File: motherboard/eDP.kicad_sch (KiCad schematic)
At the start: 1 part, among them J9 20455-040E-12 IPEX OLED

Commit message: implemented most features
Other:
- moved on the sheet: J9

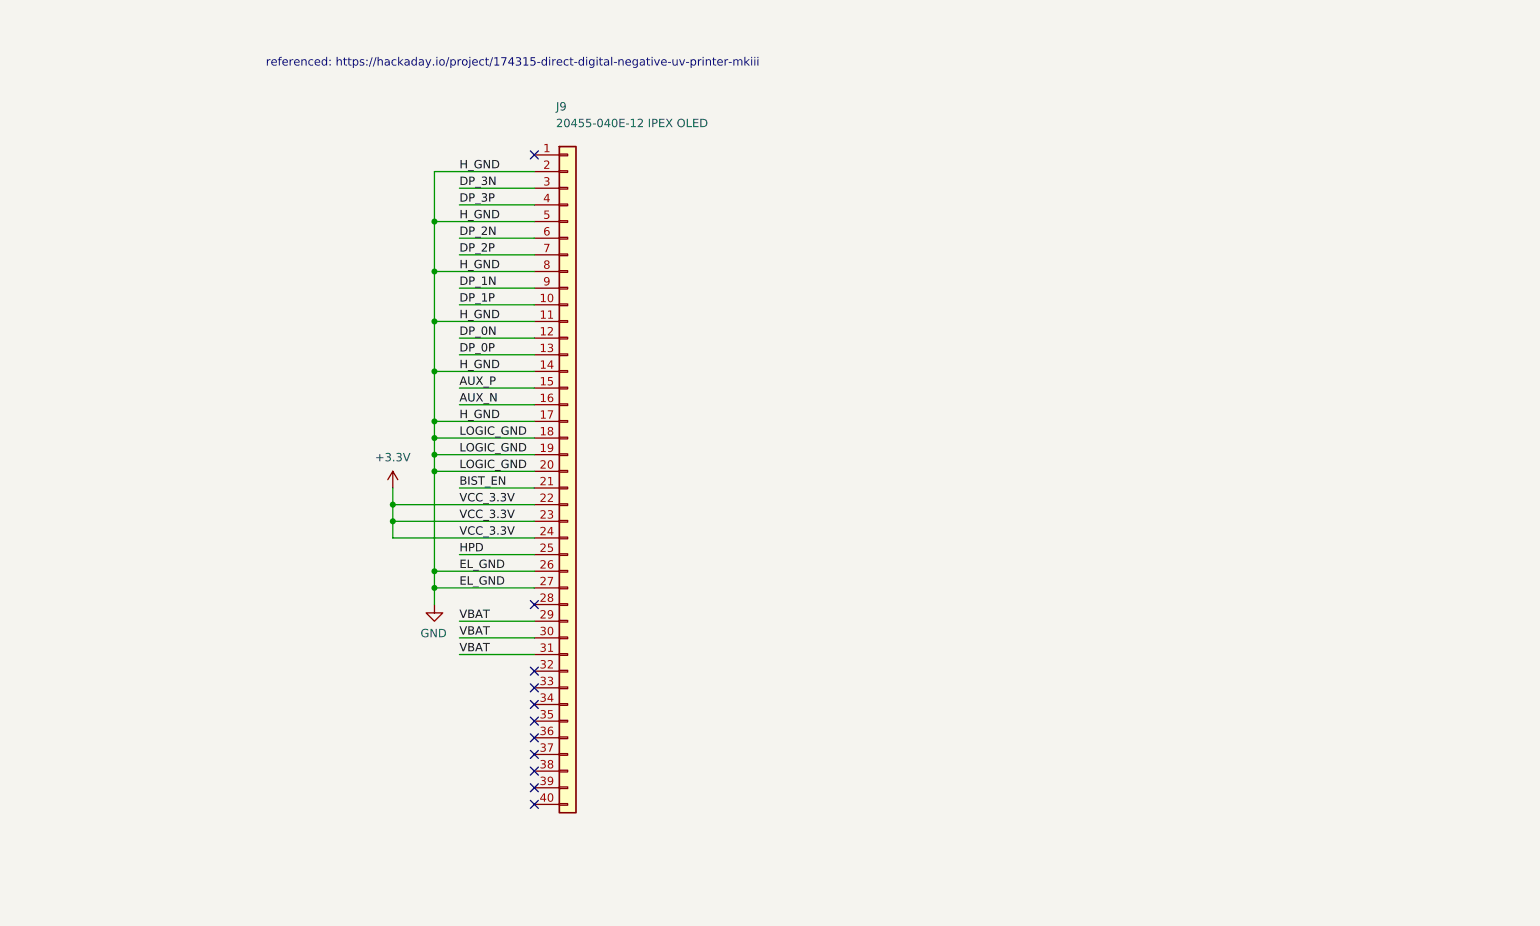
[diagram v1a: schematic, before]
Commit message: linked all footprints
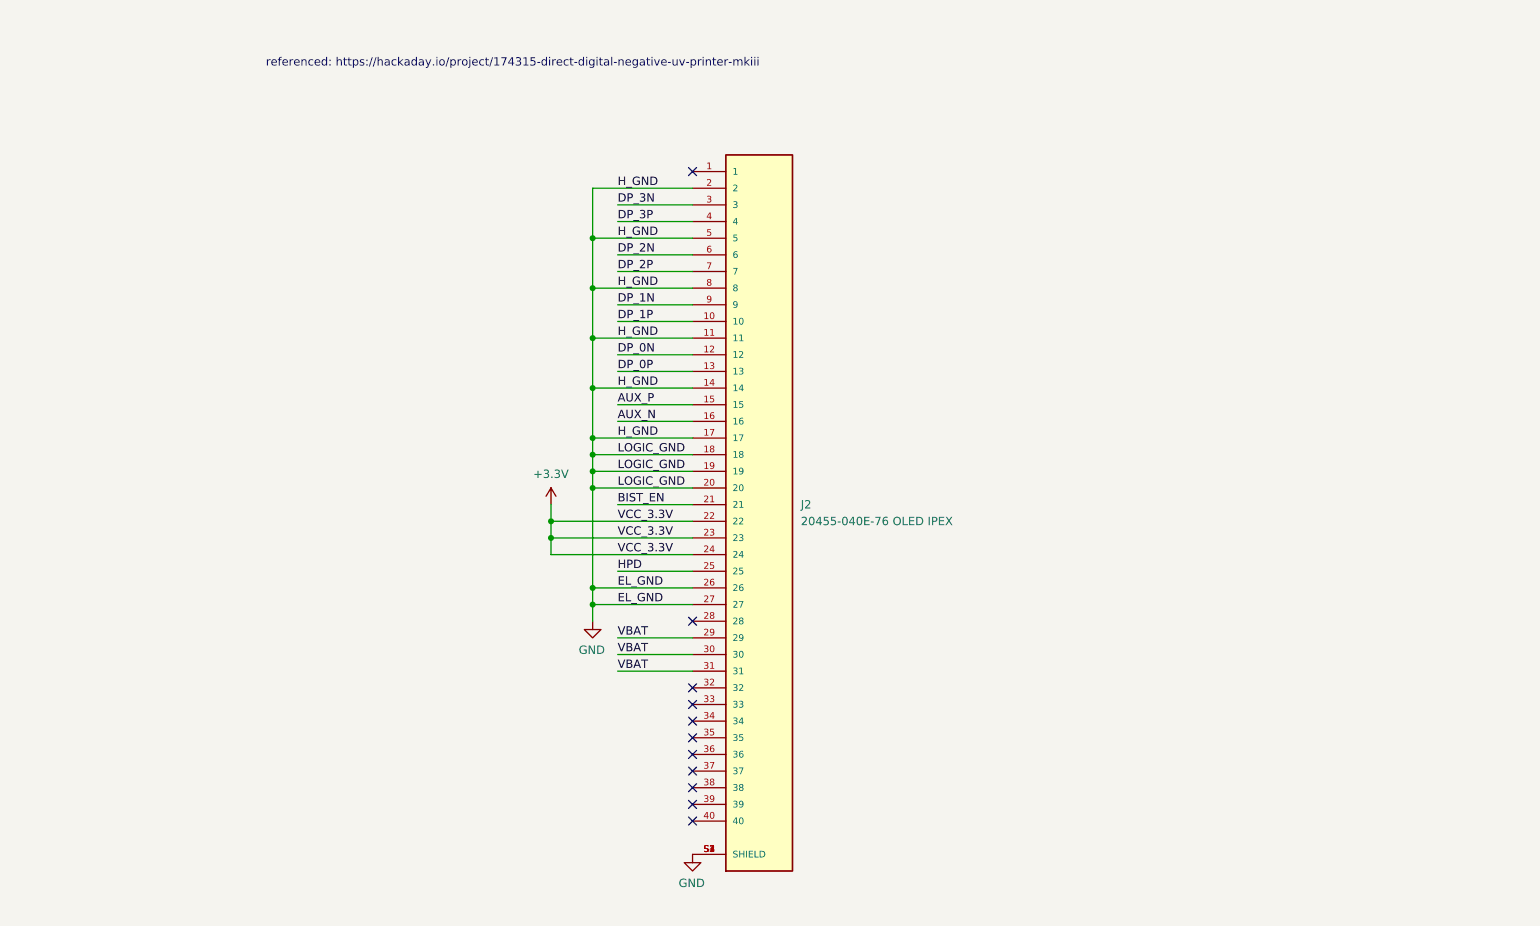
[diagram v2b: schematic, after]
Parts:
- removed J9: 20455-040E-12 IPEX OLED, symbol Connector_Generic:Conn_01x40
- added J2: 20455-040E-76 OLED IPEX, eDP_Connector:IPEX_20455-040E-76, symbol eDP_Connector:20455-040E-76
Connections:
- net +3.3V: now also J2.22, J2.23, J2.24
- net AUX_N: now also J2.16
- net AUX_P: now also J2.15
- net BIST_EN: now also J2.21
- net DP_0N: now also J2.12
- net DP_0P: now also J2.13
- net DP_1N: now also J2.9
- net DP_1P: now also J2.10
- net DP_2N: now also J2.6
- net DP_2P: now also J2.7
- net DP_3N: now also J2.3
- net DP_3P: now also J2.4
- net GND: now also J2.11, J2.14, J2.17, J2.18, J2.19, J2.2, J2.20, J2.26, J2.27, J2.5, J2.8, J2.S1 (SHIELD), J2.S2 (SHIELD), J2.S3 (SHIELD), J2.S4 (SHIELD)
- net HPD: now also J2.25
- net VBAT: now also J2.29, J2.30, J2.31

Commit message: motherboard schematic done
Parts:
- added J6: OLED EL POWER, 6P_05mm_FPC:FPC-SMD_6P-P0.50_XUNPU_FPC-05F-6PH20, symbol Connector_Generic:Conn_01x06
- added R120, R121: 0R, Resistor_SMD:R_0402_1005Metric, symbol Device:R_Small
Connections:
- net +3.3V: now also R121.1
- net BIST_EN: now also R120.1; no longer J2.21
- net GND: now also J6.1 (Pin_1), J6.2 (Pin_2), J6.3 (Pin_3)
- net HPD: no longer names the net of J2.25
- net HPD: now also R121.2
- net VBAT: no longer names the net of J2.29, J2.30, J2.31
- net VBAT: now also J6.4 (Pin_4), J6.5 (Pin_5), J6.6 (Pin_6)
- new net: J2.21, R120.2
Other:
- note added: "built in self test?"
- moved on the sheet: J2

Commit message: work preparing for routing
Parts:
- J6: symbol Connector_Generic:Conn_01x06 -> Connector_Generic_MountingPin:Conn_01x06_MountingPin
- R120: now not fitted
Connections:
- net GND: now also J6.MP (MountPin)
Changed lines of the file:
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@@
 		(in_bom yes)
 		(on_board yes)
-		(dnp no)
+		(dnp yes)
 		(fields_autoplaced yes)
 		(property "Reference" "R120"
@@
 	)
 	(symbol
-		(lib_id "Connector_Generic:Conn_01x06")
+		(lib_id "Connector_Generic_MountingPin:Conn_01x06_MountingPin")
 		(at 124.46 128.27 180)
 		(unit 1)
@@
 		(fields_autoplaced yes)
 		(property "Reference" "J6"
-			(at 124.46 114.3 0)
+			(at 121.92 125.3743 0)
 			(effects
 				(font
 					(size 1.27 1.27)
 				)
+				(justify left)
 			)
 		)
 		(property "Value" "OLED EL POWER"
-			(at 124.46 116.84 0)
+			(at 121.92 127.9143 0)
 			(effects
 				(font
 					(size 1.27 1.27)
 				)
+				(justify left)
 			)
 		)
@@
 		(pin "4"
 		)
+		(pin "MP"
+		)
 		(instances
 			(project ""
@@
 					(unit 1)
 				)
+			)
+		)
+	)
+	(symbol
+		(lib_id "eDP_adaptor_board-rescue:GND-power")
+		(at 124.46 115.57 0)
+		(mirror x)
+		(unit 1)
+		(exclude_from_sim no)
+		(in_bom yes)
+		(on_board yes)
+		(dnp no)
+		(property "Reference" "#PWR0161"
+			(at 124.46 109.22 0)
+			(effects
+				(font
+					(size 1.27 1.27)
+				)
+				(hide yes)
+			)
+		)
+		(property "Value" "GND"
+			(at 128.016 113.03 0)
+			(effects
+				(font
+					(size 1.27 1.27)
+				)
+			)
+		)
+		(property "Footprint" ""
+			(at 124.46 115.57 0)
+			(effects
+				(font
+					(size 1.27 1.27)
+				)
+				(hide yes)
+			)
+		)
+		(property "Datasheet" ""
+			(at 124.46 115.57 0)
+			(effects
+				(font
+					(size 1.27 1.27)
+				)
+				(hide yes)
+			)
+		)
+		(property "Description" ""
+			(at 124.46 115.57 0)
+			(effects
+				(font
+					(size 1.27 1.27)
+				)
+			)
+		)
+		(pin "1"
+		)
+		(instances
+			(project "motherboard"
+				(path "/025fe4d1-0305-4b34-be04-f8d9818125a4/41516588-89d4-4c4a-8d7d-a4354a401e31"
+					(reference "#PWR0161")
+					(unit 1)
+				)

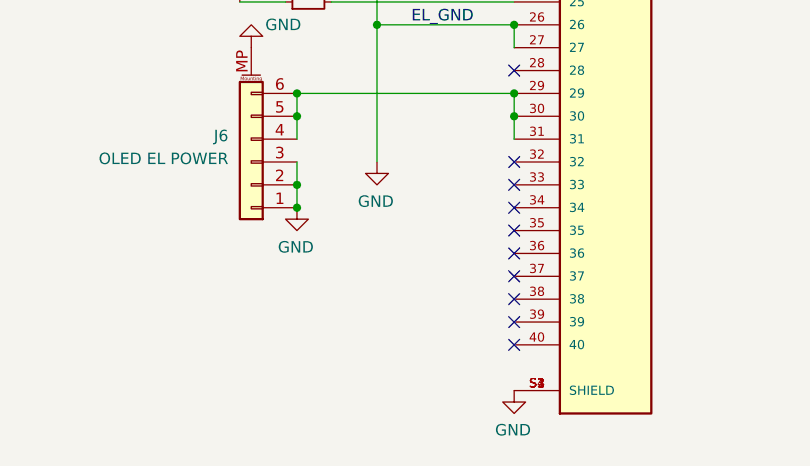
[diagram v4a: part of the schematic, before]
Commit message: component placement of I/O
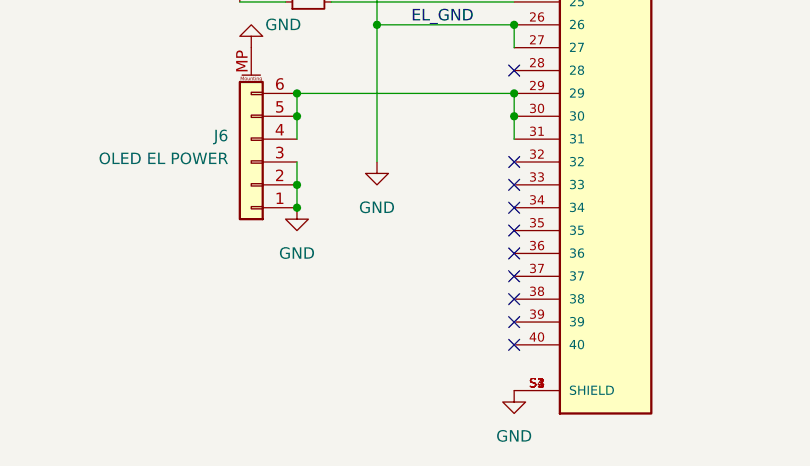
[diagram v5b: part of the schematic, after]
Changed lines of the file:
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@@
+	)
+	(junction
+		(at 129.54 133.35)
+		(diameter 0)
+		(color 0 0 0 0)
 	)
 	(junction
@@
 	)
 	(junction
-		(at 129.54 133.35)
-		(diameter 0)
-		(color 0 0 0 0)
-	)
-	(junction
 		(at 153.67 107.95)
 		(diameter 0)
@@
 	)
 	(symbol
-		(lib_id "eDP_adaptor_board-rescue:GND-power")
-		(at 129.54 133.35 0)
-		(mirror y)
+		(lib_id "power:GND")
+		(at 138.43 128.27 0)
 		(unit 1)
 		(exclude_from_sim no)
@@
 		(on_board yes)
 		(dnp no)
-		(property "Reference" "#PWR0145"
-			(at 129.54 139.7 0)
+		(fields_autoplaced yes)
+		(property "Reference" "#PWR057"
+			(at 138.43 134.62 0)
 			(effects
 				(font
@@
 		)
 		(property "Value" "GND"
-			(at 129.413 137.7442 0)
+			(at 138.43 133.35 0)
 			(effects
 				(font
@@
 		)
 		(property "Footprint" ""
-			(at 129.54 133.35 0)
+			(at 138.43 128.27 0)
 			(effects
 				(font
@@
 		)
 		(property "Datasheet" ""
-			(at 129.54 133.35 0)
-			(effects
-				(font
-					(size 1.27 1.27)
-				)
-				(hide yes)
-			)
-		)
-		(property "Description" ""
-			(at 129.54 133.35 0)
-			(effects
-				(font
-					(size 1.27 1.27)
-				)
+			(at 138.43 128.27 0)
+			(effects
+				(font
+					(size 1.27 1.27)
+				)
+				(hide yes)
+			)
+		)
+		(property "Description" "Power symbol creates a global label with name \"GND\" , ground"
+			(at 138.43 128.27 0)
+			(effects
+				(font
+					(size 1.27 1.27)
+				)
+				(hide yes)
 			)
 		)
@@
 		)
 		(instances
-			(project "motherboard"
+			(project ""
 				(path "/025fe4d1-0305-4b34-be04-f8d9818125a4/41516588-89d4-4c4a-8d7d-a4354a401e31"
-					(reference "#PWR0145")
+					(reference "#PWR057")
 					(unit 1)
 				)
@@
 	)
 	(symbol
-		(lib_id "eDP_adaptor_board-rescue:GND-power")
-		(at 153.67 153.67 0)
-		(mirror y)
+		(lib_id "power:GND")
+		(at 129.54 133.35 0)
 		(unit 1)
 		(exclude_from_sim no)
@@
 		(on_board yes)
 		(dnp no)
-		(property "Reference" "#PWR0111"
-			(at 153.67 160.02 0)
+		(fields_autoplaced yes)
+		(property "Reference" "#PWR0145"
+			(at 129.54 139.7 0)
 			(effects
 				(font
@@
 		)
 		(property "Value" "GND"
-			(at 153.543 158.0642 0)
+			(at 129.54 138.43 0)
 			(effects
 				(font
@@
 		)
 		(property "Footprint" ""
-			(at 153.67 153.67 0)
+			(at 129.54 133.35 0)
 			(effects
 				(font
@@
 		)
 		(property "Datasheet" ""
-			(at 153.67 153.67 0)
-			(effects
-				(font
-					(size 1.27 1.27)
-				)
-				(hide yes)
-			)
-		)
-		(property "Description" ""
-			(at 153.67 153.67 0)
-			(effects
-				(font
-					(size 1.27 1.27)
-				)
+			(at 129.54 133.35 0)
+			(effects
+				(font
+					(size 1.27 1.27)
+				)
+				(hide yes)
+			)
+		)
+		(property "Description" "Power symbol creates a global label with name \"GND\" , ground"
+			(at 129.54 133.35 0)
+			(effects
+				(font
+					(size 1.27 1.27)
+				)
+				(hide yes)
 			)
 		)
@@
 			(project "motherboard"
 				(path "/025fe4d1-0305-4b34-be04-f8d9818125a4/41516588-89d4-4c4a-8d7d-a4354a401e31"
-					(reference "#PWR0111")
+					(reference "#PWR0145")
 					(unit 1)
 				)
@@
 			)
 		)
-		(property "Description" "Generic connector, single row, 01x06, script generated (kicad-library-utils/schlib/autogen/connector/)"
+		(property "Description" "Generic connectable mounting pin connector, single row, 01x06, script generated (kicad-library-utils/schlib/autogen/connector/)"
 			(at 124.46 128.27 0)
 			(effects
@@
 	)
 	(symbol
-		(lib_id "eDP_adaptor_board-rescue:GND-power")
-		(at 138.43 128.27 0)
-		(mirror y)
-		(unit 1)
-		(exclude_from_sim no)
-		(in_bom yes)
-		(on_board yes)
-		(dnp no)
-		(property "Reference" "#PWR057"
-			(at 138.43 134.62 0)
-			(effects
-				(font
-					(size 1.27 1.27)
-				)
-				(hide yes)
-			)
-		)
-		(property "Value" "GND"
-			(at 138.303 132.6642 0)
-			(effects
-				(font
-					(size 1.27 1.27)
-				)
-			)
-		)
-		(property "Footprint" ""
-			(at 138.43 128.27 0)
-			(effects
-				(font
-					(size 1.27 1.27)
-				)
-				(hide yes)
-			)
-		)
-		(property "Datasheet" ""
-			(at 138.43 128.27 0)
-			(effects
-				(font
-					(size 1.27 1.27)
-				)
-				(hide yes)
-			)
-		)
-		(property "Description" ""
-			(at 138.43 128.27 0)
-			(effects
-				(font
-					(size 1.27 1.27)
-				)
-			)
-		)
-		(pin "1"
-		)
-		(instances
-			(project "motherboard"
-				(path "/025fe4d1-0305-4b34-be04-f8d9818125a4/41516588-89d4-4c4a-8d7d-a4354a401e31"
-					(reference "#PWR057")
-					(unit 1)
-				)
-			)
-		)
-	)
-	(symbol
 		(lib_id "power:+3.3V")
 		(at 123.19 110.49 0)
@@
 					(unit 1)
 				)
+			)
+		)
+	)
+	(symbol
+		(lib_id "power:GND")
+		(at 153.67 153.67 0)
+		(unit 1)
+		(exclude_from_sim no)
+		(in_bom yes)
+		(on_board yes)
+		(dnp no)
+		(fields_autoplaced yes)
+		(property "Reference" "#PWR0111"
+			(at 153.67 160.02 0)
+			(effects
+				(font
+					(size 1.27 1.27)
+				)
+				(hide yes)
+			)
+		)
+		(property "Value" "GND"
+			(at 153.67 158.75 0)
+			(effects
+				(font
+					(size 1.27 1.27)
+				)
+			)
+		)
+		(property "Footprint" ""
+			(at 153.67 153.67 0)
+			(effects
+				(font
+					(size 1.27 1.27)
+				)
+				(hide yes)
+			)
+		)
+		(property "Datasheet" ""
+			(at 153.67 153.67 0)
+			(effects
+				(font
+					(size 1.27 1.27)
+				)
+				(hide yes)
+			)
+		)
+		(property "Description" "Power symbol creates a global label with name \"GND\" , ground"
+			(at 153.67 153.67 0)
+			(effects
+				(font
+					(size 1.27 1.27)
+				)
+				(hide yes)
+			)
+		)
+		(pin "1"
+		)
+		(instances
+			(project "motherboard"
+				(path "/025fe4d1-0305-4b34-be04-f8d9818125a4/41516588-89d4-4c4a-8d7d-a4354a401e31"
+					(reference "#PWR0111")
+					(unit 1)
+				)
